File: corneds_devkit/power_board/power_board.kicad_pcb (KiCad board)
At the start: 2 copper layers, 31 parts, among them J1 Conn_01x02, J2 Conn_01x02, J3 Conn_01x08_Pin, Q1 IRLML6401, Q2 IRLML6401, U1 AMS1117-3.3, U2 AMS1117-3.3, U3 MCP73831-2-OT, U4 MCP73831-2-OT

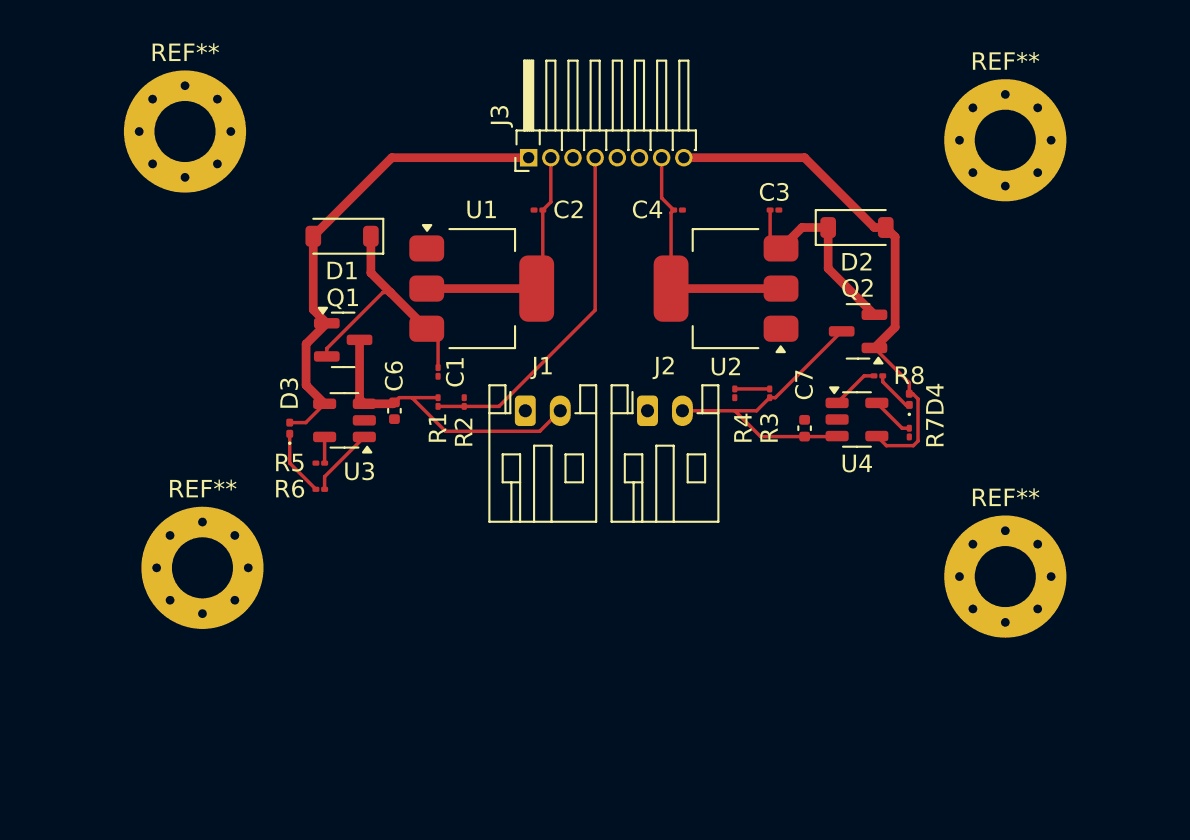
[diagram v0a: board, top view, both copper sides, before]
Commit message: finished routing power board and started on control board schematic but realized I need seperate reset lines
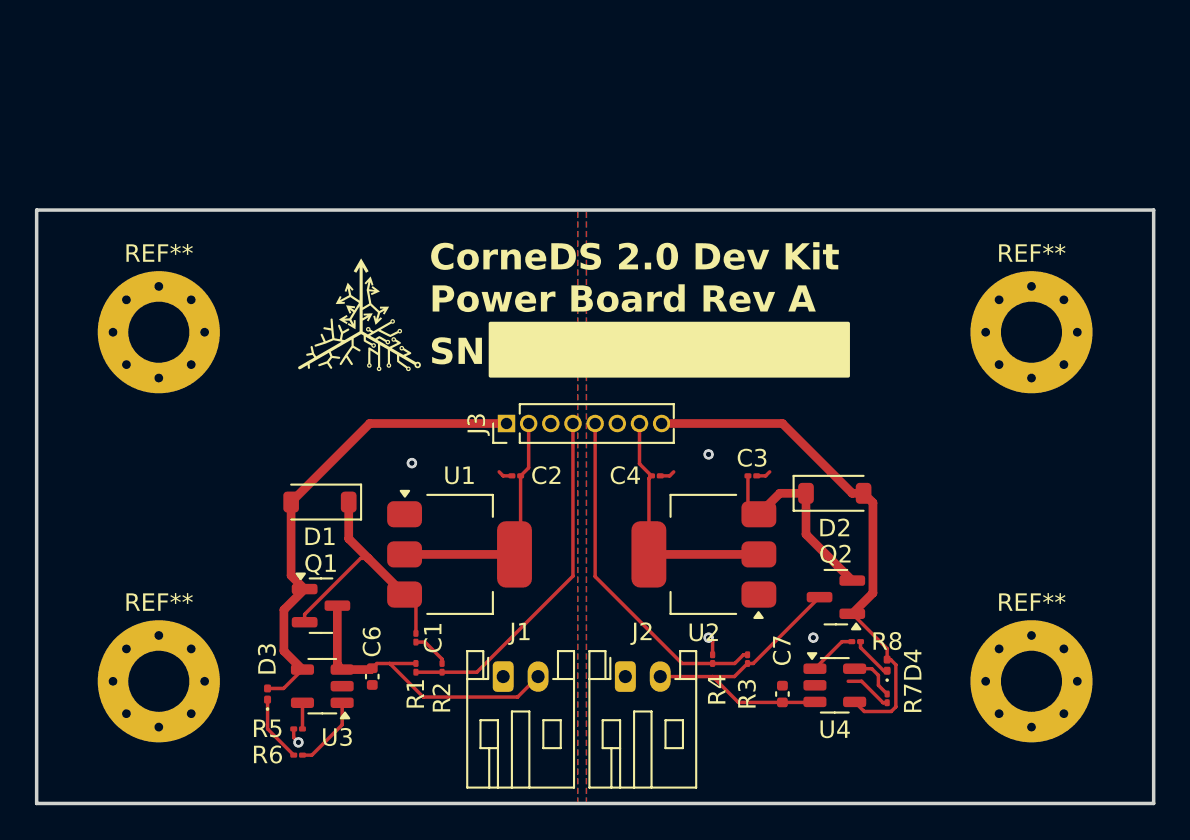
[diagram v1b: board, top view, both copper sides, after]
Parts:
- J3: footprint Connector_PinHeader_1.27mm:PinHeader_1x08_P1.27mm_Horizontal -> Connector_PinHeader_1.27mm:PinHeader_1x08_P1.27mm_Vertical
- moved C2 15.3 mm to (145.5, 88.2)
- moved C3 15.3 mm to (159.0, 88.2)
- moved C4 15.3 mm to (153.5, 88.2)
- moved C6 15.3 mm to (137.2, 99.7)
- moved C7 15.3 mm to (160.7, 100.7)
- moved D1 15.3 mm to (134.2, 89.7)
- moved D2 15.3 mm to (163.7, 89.2)
- moved D3 15.3 mm to (131.2, 100.7)
- moved D4 15.3 mm to (166.7, 99.1)
- moved J1 15.3 mm to (144.7, 99.7)
- moved J2 15.3 mm to (151.7, 99.7)
- moved J3 15.3 mm to (144.9, 85.2)
- moved Q1 15.3 mm to (134.3, 95.7)
- moved Q2 15.3 mm to (163.8, 95.2)
- moved R1 15.3 mm to (139.7, 99.2)
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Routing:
- net BAT_MEASR: track 2.00 -> 19.8 mm
- net GNDR: track 0.09 -> 5.61 mm, vias 0 -> 3
- net GNDL: track 0.00 -> 3.86 mm, vias 0 -> 2
- added copper zone on B.Cu, net GNDL
- added copper zone on F.Cu, net GNDL
- added copper zone on B.Cu, net GNDR
- added copper zone on F.Cu, net GNDR
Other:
- board outline added: 64 x 34 mm
- board text added: "CorneDS 2.0 Dev Kit Power Board Rev A"
- board text added: "Mar 13, 2025"
- board text added: "Mar 14, 2025"
- board text added: "SN"

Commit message: ordered devkit rev A
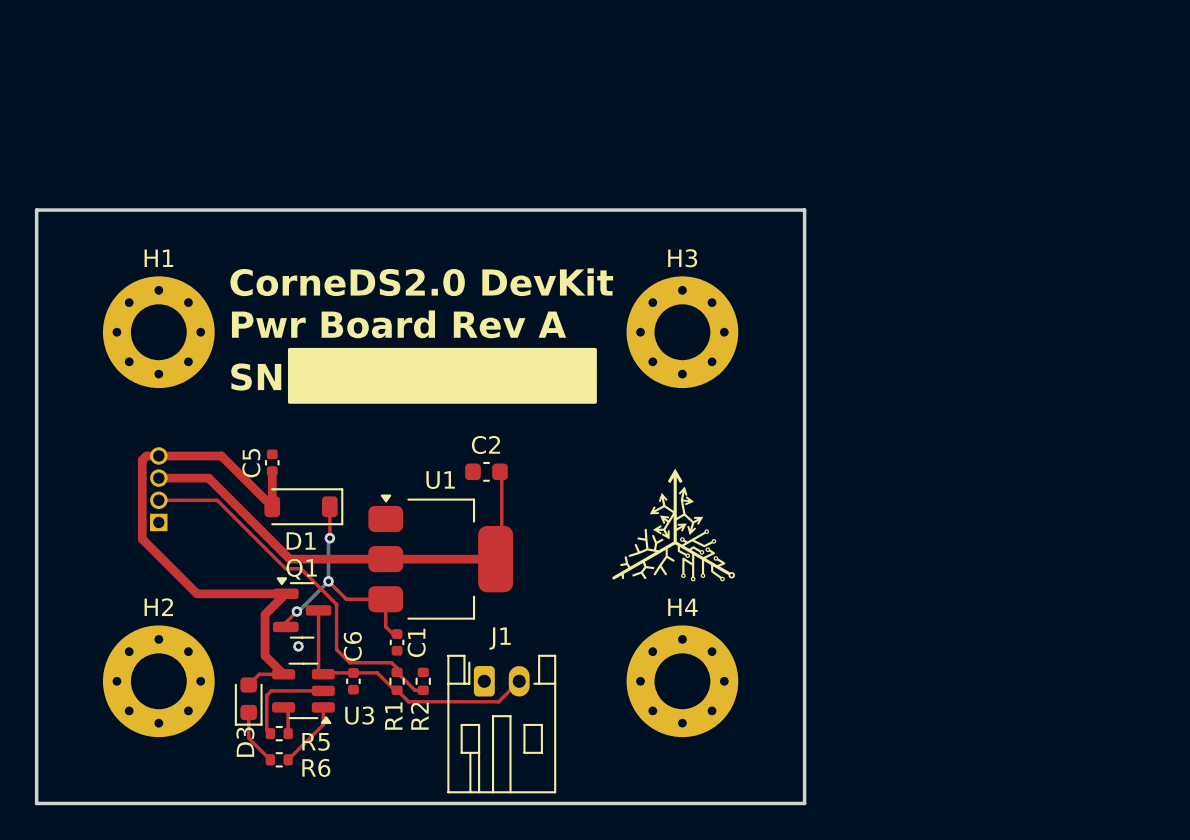
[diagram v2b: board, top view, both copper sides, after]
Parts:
- removed C3: 10uF, Capacitor_SMD:C_01005_0402Metric
- removed C4: 22uF, Capacitor_SMD:C_01005_0402Metric
- removed C7: 4.7uF, Capacitor_SMD:C_0402_1005Metric
- removed D2: 1N4148W, Diode_SMD:D_SOD-123
- removed D4: LTST-C190KRKT, LED_SMD:LED_0201_0603Metric
- removed J3: Conn_01x08_Pin, Connector_PinHeader_1.27mm:PinHeader_1x08_P1.27mm_Vertical
- removed Q2: IRLML6401, Package_TO_SOT_SMD:SOT-23
- removed R3, R4: 100kOhm, Resistor_SMD:R_01005_0402Metric
- removed R7: 2kOhm, Resistor_SMD:R_01005_0402Metric
- removed R8: 470Ohm, Resistor_SMD:R_01005_0402Metric
- removed REF** (x4): MountingHole_3.5mm_Pad_Via, MountingHole:MountingHole_3.5mm_Pad_Via
- removed U2: AMS1117-3.3, Package_TO_SOT_SMD:SOT-223-3_TabPin2
- removed U4: MCP73831-2-OT, Package_TO_SOT_SMD:SOT-23-5
- added C5: 4.7uF, Capacitor_SMD:C_0402_1005Metric, F.Cu at (131.5, 87.5)
- added H1: ~, MountingHole:MountingHole_3.2mm_M3_Pad_Via, F.Cu at (125.0, 80.0)
- added H2: ~, MountingHole:MountingHole_3.2mm_M3_Pad_Via, F.Cu at (125.0, 100.0)
- added H3: ~, MountingHole:MountingHole_3.2mm_M3_Pad_Via, F.Cu at (155.0, 80.0)
- added H4: ~, MountingHole:MountingHole_3.2mm_M3_Pad_Via, F.Cu at (155.0, 100.0)
- C1: footprint Capacitor_SMD:C_01005_0402Metric -> Capacitor_SMD:C_0402_1005Metric
- C2: footprint Capacitor_SMD:C_01005_0402Metric -> Capacitor_SMD:C_0603_1608Metric
- D3: footprint LED_SMD:LED_0201_0603Metric -> LED_SMD:LED_0603_1608Metric
- J1: value Conn_01x02 -> BAT
- J2: value Conn_01x02 -> ~; footprint Connector_JST:JST_PH_S2B-PH-K_1x02_P2.00mm_Horizontal -> Connector_PinHeader_1.27mm:PinHeader_1x04_P1.27mm_Vertical; moved to B.Cu
- R1, R2, R5, R6: footprint Resistor_SMD:R_01005_0402Metric -> Resistor_SMD:R_0402_1005Metric
- moved J2 28.2 mm to (125.0, 90.9)
- moved C2 1.72 mm to (143.8, 88.0)
- moved R1 1.33 mm to (138.7, 100.0), turned to 90 degrees
- moved R2 1.33 mm to (140.2, 100.0)
- moved U3 1.11 mm to (133.3, 100.5)
- moved C1 1.11 mm to (138.7, 97.8)
- moved C6 1.11 mm to (136.2, 100.0)
- moved D1 1.11 mm to (133.2, 90.0)
- moved D3 1.11 mm to (130.2, 101.0)
- moved J1 1.11 mm to (143.7, 100.0)
- moved Q1 1.11 mm to (133.2, 95.9)
- moved R5 1.11 mm to (131.9, 103.0)
- moved R6 1.11 mm to (131.9, 104.5)
- moved U1 1.11 mm to (141.2, 93.0)
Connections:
- net BAT+L renamed BAT+
- C1 pad 2: GNDL -> GND
- C2 pad 1: 3_3VL -> 3V3
- C2 pad 2: GNDL -> GND
- C6 pad 2: GNDL -> GND
- D1 pad 2: USB_5VL -> USB_5V
- D3 pad 2: USB_5VL -> USB_5V
- J1 pad 1: GNDL -> GND
- J2 pad 1: GNDR -> GND
- J2 pad 2: BAT+R -> BAT_MEAS
- Q1 pad 1: USB_5VL -> USB_5V
- R1 pad 2: BAT_MEASL -> BAT_MEAS
- R2 pad 1: BAT_MEASL -> BAT_MEAS
- R2 pad 2: GNDL -> GND
- R5 pad 1: GNDL -> GND
- U1 pad 1: GNDL -> GND
- U1 pad 2: 3_3VL -> 3V3
- U3 pad 2: GNDL -> GND
- U3 pad 4: USB_5VL -> USB_5V
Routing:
- net USB_5V: track 0.00 -> 32.6 mm
- net USB_5VR: track 30.0 -> 0.00 mm
- net USB_5VL: track 27.5 -> 0.00 mm
- net 3V3: track 0.00 -> 25.9 mm
- net BAT_MEAS: track 0.00 -> 21.3 mm
- net BAT_MEASL: track 20.0 -> 0.00 mm
- net BAT_MEASR: track 19.8 -> 0.00 mm
- net BAT+R: track 17.5 -> 0.00 mm
- net 3_3VR: track 14.1 -> 0.00 mm
- net 3_3VL: track 14.1 -> 0.00 mm
- net Net-(D2-K): track 11.8 -> 0.00 mm
- net GND: track 0.00 -> 5.62 mm, vias 0 -> 1
- net GNDR: track 5.61 -> 0.00 mm, vias 3 -> 0
- net GNDL: track 3.86 -> 0.00 mm, vias 2 -> 0
- net Net-(U4-PROG): track 2.80 -> 0.00 mm
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- added copper zone on B.Cu, net GND
- added copper zone on F.Cu, net GND
- removed copper zone on B.Cu, net GNDL
- removed copper zone on F.Cu, net GNDL
- removed copper zone on B.Cu, net GNDR
- removed copper zone on F.Cu, net GNDR
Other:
- board size 64 x 34 mm -> 44 x 34 mm
- board text added: "CorneDS2.0 DevKit Pwr Board Rev A"
- board text added: "Jul 30, 2025"
- board text removed: "CorneDS 2.0 Dev Kit Power Board Rev A"
- board text removed: "Mar 13, 2025"
- board text removed: "Mar 14, 2025"
